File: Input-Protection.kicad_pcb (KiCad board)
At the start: 2 copper layers, 39 parts, among them IC501 AZV3002S-13, J101 EBWA-02-B, J102 KLDX-0202-B, J103 EBWA-02-B, J104 KLDX-0202-B, Q101 MCU18P10Y-TP, Q401 BC846, Q402 MCU18P10Y-TP, U301 LM4040DBZ-5

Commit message: fix: reset pcb layout
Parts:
- removed D101, D401: D3Z10BF-7, Diode_SMD:D_SOD-323_HandSoldering
- removed D501, D502: 1N4148WS, Diode_SMD:D_SOD-323
- removed IC501: AZV3002S-13, Package_SO:Diodes_SO-8EP
- removed ID601: BOARD_STACKUP_MARKER, RD-Symbols-Silkscreen:STACKUP_ID_2L_SML
- removed J101, J103: EBWA-02-B, TerminalBlock_Phoenix:TerminalBlock_Phoenix_MKDS-1-2-3.81_1x02_P3.81mm_Horizontal
- removed J102, J104: KLDX-0202-B, Connector_BarrelJack:BarrelJack_Kycon_KLDX-0202-xC_Horizontal
- removed Q101, Q402: MCU18P10Y-TP, MCU18P10Y-TP:DPAK_MCC
- removed Q401: BC846, Package_TO_SOT_SMD:SOT-23
- removed R101, R102, R402, R403, R503: 100k, Resistor_SMD:R_1206_3216Metric_Pad1.30x1.75mm_HandSolder
- removed R201: 39k, Resistor_SMD:R_1206_3216Metric_Pad1.30x1.75mm_HandSolder
- removed R202, R204, R301, R302, R303, R401: 10k, Resistor_SMD:R_1206_3216Metric_Pad1.30x1.75mm_HandSolder
- removed R203: 58k, Resistor_SMD:R_1206_3216Metric_Pad1.30x1.75mm_HandSolder
- removed R404, R504, R505: 1M, Resistor_SMD:R_1206_3216Metric_Pad1.30x1.75mm_HandSolder
- removed R501, R502: 1k, Resistor_SMD:R_1206_3216Metric_Pad1.30x1.75mm_HandSolder
- removed TP101: VIN, TestPoint:TestPoint_Pad_D2.5mm
- removed TP102: VPROT, TestPoint:TestPoint_Pad_D2.5mm
- removed TP201: V_OV, TestPoint:TestPoint_Pad_D2.5mm
- removed TP202: V_UV, TestPoint:TestPoint_Pad_D2.5mm
- removed TP301: VREF_2V5, TestPoint:TestPoint_Pad_D2.5mm
- removed TP302: VCC_5V, TestPoint:TestPoint_Pad_D2.5mm
- removed TP401: VOUT, TestPoint:TestPoint_Pad_D2.5mm
- removed U301: LM4040DBZ-5, Package_TO_SOT_SMD:SOT-23

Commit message: feat: Added some design notes, fixed some values in line with sim
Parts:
- added C401: 10n, Capacitor_SMD:C_0603_1608Metric_Pad1.08x0.95mm_HandSolder, F.Cu at (170.5, 61.3)
- added C402: 100n, Capacitor_SMD:C_0603_1608Metric_Pad1.08x0.95mm_HandSolder, F.Cu at (170.5, 63.8)
- added C601: 10n, Capacitor_SMD:C_0603_1608Metric_Pad1.08x0.95mm_HandSolder, F.Cu at (170.5, 66.3)
- added C602: 10n, Capacitor_SMD:C_0603_1608Metric_Pad1.08x0.95mm_HandSolder, F.Cu at (170.5, 68.8)
- added D201: D3Z10BF-7, Diode_SMD:D_SOD-323_HandSoldering, F.Cu at (135.0, 98.9)
- added D501: D3Z10BF-7, Diode_SMD:D_SOD-323_HandSoldering, F.Cu at (135.0, 101.9)
- added D701: 1N4148WS, Diode_SMD:D_SOD-323, F.Cu at (139.7, 98.9)
- added D702: 1N4148WS, Diode_SMD:D_SOD-323, F.Cu at (139.7, 101.9)
- added FID901: FIDUCIAL, Fiducial:Fiducial_Cross_0.5mm_Mask2mm, F.Cu at (153.5, 78.3)
- added FID902: FIDUCIAL, Fiducial:Fiducial_Cross_0.5mm_Mask2mm, F.Cu at (153.5, 81.9)
- added FID903: FIDUCIAL, Fiducial:Fiducial_Cross_0.5mm_Mask2mm, F.Cu at (153.5, 85.4)
- added H901: MOUNT_M3, MountingHole:MountingHole_3.2mm_M3_ISO7380_Pad, F.Cu at (148.1, 80.2)
- added H902: MOUNT_M3, MountingHole:MountingHole_3.2mm_M3_ISO7380_Pad, F.Cu at (148.1, 87.4)
- added H903: MOUNT_M3, MountingHole:MountingHole_3.2mm_M3_ISO7380_Pad, F.Cu at (148.1, 94.7)
- added H904: MOUNT_M3, MountingHole:MountingHole_3.2mm_M3_ISO7380_Pad, F.Cu at (148.1, 101.9)
- added ID901: BOARD_STACKUP_MARKER, RD-Symbols-Silkscreen:STACKUP_ID_2L_SML, F.Cu at (165.0, 104.0)
- added J101: KLDX-0202-B, Connector_BarrelJack:BarrelJack_Kycon_KLDX-0202-xC_Horizontal, F.Cu at (142.5, 65.5)
- added J102: EBWA-02-B, TerminalBlock_Phoenix:TerminalBlock_Phoenix_MKDS-1-2-3.81_1x02_P3.81mm_Horizontal, F.Cu at (165.3, 81.3)
- added J103: EBWA-02-B, TerminalBlock_Phoenix:TerminalBlock_Phoenix_MKDS-1-2-3.81_1x02_P3.81mm_Horizontal, F.Cu at (165.3, 90.9)
- added J104: KLDX-0202-B, Connector_BarrelJack:BarrelJack_Kycon_KLDX-0202-xC_Horizontal, F.Cu at (142.5, 77.8)
- added Q201: MCU18P10Y-TP, MCU18P10Y-TP:DPAK_MCC, F.Cu at (131.7, 90.3)
- added Q501: BC846, Package_TO_SOT_SMD:SOT-23, F.Cu at (130.0, 99.7)
- added Q502: MCU18P10Y-TP, MCU18P10Y-TP:DPAK_MCC, F.Cu at (140.1, 90.3)
- added R201: 100k, Resistor_SMD:R_1206_3216Metric_Pad1.30x1.75mm_HandSolder, F.Cu at (147.5, 61.7)
- added R202: 100k, Resistor_SMD:R_1206_3216Metric_Pad1.30x1.75mm_HandSolder, F.Cu at (147.5, 65.0)
- added R301: 39.2k, Resistor_SMD:R_1206_3216Metric_Pad1.30x1.75mm_HandSolder, F.Cu at (147.5, 68.3)
- added R302: 10k, Resistor_SMD:R_1206_3216Metric_Pad1.30x1.75mm_HandSolder, F.Cu at (147.5, 71.6)
- added R303: 56.2k, Resistor_SMD:R_1206_3216Metric_Pad1.30x1.75mm_HandSolder, F.Cu at (147.5, 74.9)
- added R304: 10k, Resistor_SMD:R_1206_3216Metric_Pad1.30x1.75mm_HandSolder, F.Cu at (153.4, 61.7)
- added R401: 100k, Resistor_SMD:R_1206_3216Metric_Pad1.30x1.75mm_HandSolder, F.Cu at (153.4, 65.0)
- added R402: 100k, Resistor_SMD:R_1206_3216Metric_Pad1.30x1.75mm_HandSolder, F.Cu at (153.4, 68.3)
- added R403: 10k, Resistor_SMD:R_1206_3216Metric_Pad1.30x1.75mm_HandSolder, F.Cu at (153.4, 71.6)
- added R501: 10k, Resistor_SMD:R_1206_3216Metric_Pad1.30x1.75mm_HandSolder, F.Cu at (153.4, 74.9)
- added R502: 100k, Resistor_SMD:R_1206_3216Metric_Pad1.30x1.75mm_HandSolder, F.Cu at (159.4, 61.7)
- added R503: 100k, Resistor_SMD:R_1206_3216Metric_Pad1.30x1.75mm_HandSolder, F.Cu at (159.4, 65.0)
- added R504: 1M, Resistor_SMD:R_1206_3216Metric_Pad1.30x1.75mm_HandSolder, F.Cu at (159.4, 68.3)
- added R601: 1k, Resistor_SMD:R_1206_3216Metric_Pad1.30x1.75mm_HandSolder, F.Cu at (159.4, 71.6)
- added R602: 1k, Resistor_SMD:R_1206_3216Metric_Pad1.30x1.75mm_HandSolder, F.Cu at (159.4, 74.9)
- added R701: 470, Resistor_SMD:R_1206_3216Metric_Pad1.30x1.75mm_HandSolder, F.Cu at (165.3, 61.7)
- added R702: 470, Resistor_SMD:R_1206_3216Metric_Pad1.30x1.75mm_HandSolder, F.Cu at (165.3, 65.0)
- added R703: 47k, Resistor_SMD:R_1206_3216Metric_Pad1.30x1.75mm_HandSolder, F.Cu at (165.3, 68.3)
- added R801: 1M, Resistor_SMD:R_1206_3216Metric_Pad1.30x1.75mm_HandSolder, F.Cu at (165.3, 71.6)
- added R802: 1M, Resistor_SMD:R_1206_3216Metric_Pad1.30x1.75mm_HandSolder, F.Cu at (165.3, 74.9)
- added TP101: GND, TestPoint:TestPoint_Pad_D1.5mm, F.Cu at (153.5, 89.0)
- added TP102: VIN, TestPoint:TestPoint_Pad_D1.5mm, F.Cu at (153.5, 92.5)
- added TP103: VOUT, TestPoint:TestPoint_Pad_D1.5mm, F.Cu at (153.5, 96.1)
- added TP104: GND, TestPoint:TestPoint_Pad_D1.5mm, F.Cu at (157.1, 78.3)
- added TP202: VPROT, TestPoint:TestPoint_Pad_D1.5mm, F.Cu at (157.1, 81.9)
- added TP301: GND, TestPoint:TestPoint_Pad_D1.5mm, F.Cu at (157.1, 85.4)
- added TP302: VSENSE_12V, TestPoint:TestPoint_Pad_D1.5mm, F.Cu at (157.1, 89.0)
- added TP303: VSENSE_17V, TestPoint:TestPoint_Pad_D1.5mm, F.Cu at (157.1, 92.5)
- added TP401: VREF_2V5, TestPoint:TestPoint_Pad_D1.5mm, F.Cu at (157.1, 96.1)
- added TP402: VCC_5V, TestPoint:TestPoint_Pad_D1.5mm, F.Cu at (160.6, 78.3)
- added TP403: GND, TestPoint:TestPoint_Pad_D1.5mm, F.Cu at (160.6, 81.9)
- added TP601: 12V_OK, TestPoint:TestPoint_Pad_D1.5mm, F.Cu at (160.6, 85.4)
- added TP602: 17V_OK, TestPoint:TestPoint_Pad_D1.5mm, F.Cu at (160.6, 89.0)
- added TP701: EN_OK, TestPoint:TestPoint_Pad_D1.5mm, F.Cu at (160.6, 92.5)
- added U401: LM4040DBZ-5, Package_TO_SOT_SMD:SOT-23, F.Cu at (130.0, 104.1)
- added U601: AZV3002S-13, Package_SO:Diodes_SO-8EP, F.Cu at (166.4, 99.3)

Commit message: feat: preliminary pcb layout
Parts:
- removed C601, C602: 10n, Capacitor_SMD:C_0603_1608Metric_Pad1.08x0.95mm_HandSolder
- removed D701, D702: 1N4148WS, Diode_SMD:D_SOD-323
- removed Q501: BC846, Package_TO_SOT_SMD:SOT-23
- removed Q502: MCU18P10Y-TP, MCU18P10Y-TP:DPAK_MCC
- removed R701, R702: 470, Resistor_SMD:R_1206_3216Metric_Pad1.30x1.75mm_HandSolder
- removed R703: 47k, Resistor_SMD:R_1206_3216Metric_Pad1.30x1.75mm_HandSolder
- removed R801, R802: 1M, Resistor_SMD:R_1206_3216Metric_Pad1.30x1.75mm_HandSolder
- removed TP202: VPROT, TestPoint:TestPoint_Pad_D1.5mm
- removed TP402: VCC_5V, TestPoint:TestPoint_Pad_D1.5mm
- removed TP601: 12V_OK, TestPoint:TestPoint_Pad_D1.5mm
- removed TP602: 17V_OK, TestPoint:TestPoint_Pad_D1.5mm
- removed TP701: EN_OK, TestPoint:TestPoint_Pad_D1.5mm
- removed U601: AZV3002S-13, Package_SO:Diodes_SO-8EP
- added C501: 10n, Capacitor_SMD:C_0603_1608Metric_Pad1.08x0.95mm_HandSolder, F.Cu at (161.0, 87.7)
- added C502: 10n, Capacitor_SMD:C_0603_1608Metric_Pad1.08x0.95mm_HandSolder, F.Cu at (161.0, 77.5)
- added D502: 1N4148WS, Diode_SMD:D_SOD-323, F.Cu at (155.6, 93.3)
- added D601: D3Z10BF-7, Diode_SMD:D_SOD-323_HandSoldering, F.Cu at (171.6, 85.7)
- added Q601: BC846, Package_TO_SOT_SMD:SOT-23, F.Cu at (169.1, 94.8)
- added Q602: MCU18P10Y-TP, MCU18P10Y-TP:DPAK_MCC, F.Cu at (171.6, 77.4)
- added R505: 47k, Resistor_SMD:R_1206_3216Metric_Pad1.30x1.75mm_HandSolder, F.Cu at (148.6, 89.2)
- added R506: 1M, Resistor_SMD:R_1206_3216Metric_Pad1.30x1.75mm_HandSolder, F.Cu at (152.6, 89.2)
- added R507: 1M, Resistor_SMD:R_1206_3216Metric_Pad1.30x1.75mm_HandSolder, F.Cu at (152.6, 75.9)
- added R603: 100k, Resistor_SMD:R_1206_3216Metric_Pad1.30x1.75mm_HandSolder, F.Cu at (171.6, 90.7)
- added R604: 1M, Resistor_SMD:R_1206_3216Metric_Pad1.30x1.75mm_HandSolder, F.Cu at (171.6, 68.2)
- added TP201: VPROT, TestPoint:TestPoint_Pad_D1.5mm, F.Cu at (133.1, 94.7)
- added TP501: 12V_OK, TestPoint:TestPoint_Pad_D1.0mm, F.Cu at (152.1, 85.4)
- added TP502: 17V_OK, TestPoint:TestPoint_Pad_D1.0mm, F.Cu at (153.2, 72.4)
- added TP503: EN_OK, TestPoint:TestPoint_Pad_D1.5mm, F.Cu at (169.1, 98.9)
- added U501: AZV3002S-13, Package_SO:Diodes_SO-8EP, F.Cu at (157.3, 82.5)
- D501: value D3Z10BF-7 -> 1N4148WS; footprint Diode_SMD:D_SOD-323_HandSoldering -> Diode_SMD:D_SOD-323
- R501: value 10k -> 1k
- R502: value 100k -> 1k
- R503: value 100k -> 470
- R504: value 1M -> 470
- R601: value 1k -> 10k
- R602: value 1k -> 100k
- TP101, TP104, TP301: footprint TestPoint:TestPoint_Pad_D1.5mm -> TestPoint:TestPoint_THTPad_2.0x2.0mm_Drill1.0mm
- TP401: footprint TestPoint:TestPoint_Pad_D1.5mm -> TestPoint:TestPoint_Pad_D1.0mm
- TP403: value GND -> VCC_5V; footprint TestPoint:TestPoint_Pad_D1.5mm -> TestPoint:TestPoint_Pad_D1.0mm
- U401: value LM4040DBZ-5 -> LM4040N-5.0
- moved ID901 55.9 mm to (124.3, 65.7)
- moved H903 49.0 mm to (187.6, 65.7)
- moved J102 48.9 mm to (116.6, 85.7), turned to -90 degrees
- moved H904 39.7 mm to (187.6, 97.7)
- moved R201 38.1 mm to (128.5, 94.7)
- moved FID902 36.5 mm to (120.6, 97.7)
- moved D501 36.5 mm to (155.6, 71.7), turned to 90 degrees
- moved H901 35.7 mm to (115.6, 65.7)
- moved FID901 35.3 mm to (120.6, 65.7)
- moved FID903 35.1 mm to (182.6, 65.7)
- moved J104 34.5 mm to (176.9, 75.2), turned to 180 degrees
- moved H902 34.1 mm to (115.6, 97.7)
- moved C402 31.1 mm to (146.4, 83.4), turned to -90 degrees
- moved R202 30.2 mm to (131.6, 90.7)
- moved TP102 29.2 mm to (125.3, 84.8), turned to 180 degrees
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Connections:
- net VIN renamed /ARCHITECTURE/1. INTERCONNECTS/VIN
- D201 pad 1: VPROT -> /ARCHITECTURE/2. POLARITY PROTECTION/VPROT
- D501 pad 1: VPROT -> Net-(D501-K)
- D501 pad 2: Net-(D501-A) -> /ARCHITECTURE/5. COMPARATOR/EN_OK
- J103 pad 1: VOUT -> GND
- J103 pad 2: GND -> /ARCHITECTURE/1. INTERCONNECTS/VOUT
- J104 pad 1: VOUT -> /ARCHITECTURE/1. INTERCONNECTS/VOUT
- Q201 pad 3: VPROT -> /ARCHITECTURE/2. POLARITY PROTECTION/VPROT
- R202 pad 2: VPROT -> /ARCHITECTURE/2. POLARITY PROTECTION/VPROT
- R301 pad 1: VSENSE_12V -> /ARCHITECTURE/3. SENSING/VSENSE_12V
- R301 pad 2: VPROT -> /ARCHITECTURE/2. POLARITY PROTECTION/VPROT
- R302 pad 2: VSENSE_12V -> /ARCHITECTURE/3. SENSING/VSENSE_12V
- R303 pad 1: VSENSE_17V -> /ARCHITECTURE/3. SENSING/VSENSE_17V
- R303 pad 2: VPROT -> /ARCHITECTURE/2. POLARITY PROTECTION/VPROT
- R304 pad 2: VSENSE_17V -> /ARCHITECTURE/3. SENSING/VSENSE_17V
- R403 pad 2: VPROT -> /ARCHITECTURE/2. POLARITY PROTECTION/VPROT
- R501 pad 1: Net-(Q501-B) -> Net-(U501A-+)
- R501 pad 2: EN_OK -> /ARCHITECTURE/3. SENSING/VSENSE_12V
- R502 pad 1: Net-(Q501-B) -> Net-(U501B--)
- R502 pad 2: GND -> /ARCHITECTURE/3. SENSING/VSENSE_17V
- R503 pad 1: Net-(D501-A) -> Net-(D501-K)
- R503 pad 2: VPROT -> /ARCHITECTURE/5. COMPARATOR/17V_OK
- R504 pad 1: VOUT -> Net-(D502-K)
- R504 pad 2: GND -> /ARCHITECTURE/5. COMPARATOR/12V_OK
- R601 pad 1: Net-(U601A-+) -> Net-(Q601-B)
- R601 pad 2: VSENSE_12V -> /ARCHITECTURE/5. COMPARATOR/EN_OK
- R602 pad 1: Net-(U601B--) -> Net-(Q601-B)
- R602 pad 2: VSENSE_17V -> GND
- TP103 pad 1: VOUT -> /ARCHITECTURE/1. INTERCONNECTS/VOUT
- TP302 pad 1: VSENSE_12V -> /ARCHITECTURE/3. SENSING/VSENSE_12V
- TP303 pad 1: VSENSE_17V -> /ARCHITECTURE/3. SENSING/VSENSE_17V
- TP403 pad 1: GND -> VCC_5V
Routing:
- net /ARCHITECTURE/5. COMPARATOR/EN_OK: track 0.00 -> 59.5 mm
- net VREF_2V5: track 0.00 -> 31.8 mm
- net /ARCHITECTURE/3. SENSING/VSENSE_17V: track 0.00 -> 22.6 mm
- net /ARCHITECTURE/3. SENSING/VSENSE_12V: track 0.00 -> 20.3 mm
- net GND: track 0.00 -> 10.2 mm, vias 0 -> 8
- net /ARCHITECTURE/5. COMPARATOR/17V_OK: track 0.00 -> 5.98 mm
- net /ARCHITECTURE/5. COMPARATOR/12V_OK: track 0.00 -> 3.49 mm
- net /ARCHITECTURE/2. POLARITY PROTECTION/VPROT: vias 0 -> 6
- added copper zone on F.Cu, net /ARCHITECTURE/1. INTERCONNECTS/VIN
- added copper zone on F.Cu, net /ARCHITECTURE/1. INTERCONNECTS/VOUT
- added copper zone on B.Cu, net /ARCHITECTURE/2. POLARITY PROTECTION/VPROT
- added copper zone on F.Cu, net /ARCHITECTURE/2. POLARITY PROTECTION/VPROT
- added copper zone on F.Cu, net /ARCHITECTURE/3. SENSING/VSENSE_12V
- added copper zone on F.Cu, net /ARCHITECTURE/3. SENSING/VSENSE_17V
- added copper zone on F.Cu, net /ARCHITECTURE/5. COMPARATOR/12V_OK
- added copper zone on F.Cu, net /ARCHITECTURE/5. COMPARATOR/17V_OK
- added copper zone on B.Cu, net GND
- added copper zone on F.Cu, net GND
- added copper zone on F.Cu, net Net-(D201-A)
- added copper zone on F.Cu, net Net-(D501-K)
- added copper zone on F.Cu, net Net-(D502-K)
- added copper zone on F.Cu, net Net-(D601-A)
- added copper zone on F.Cu, net Net-(Q601-B)
- added copper zone on F.Cu, net Net-(U501A-+)
- added copper zone on F.Cu, net Net-(U501B--)
- added copper zone on F.Cu, net VCC_5V
- added copper zone on F.Cu, net VREF_2V5
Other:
- board outline added: 80 x 40 mm
- board text added: "A"
- board text added: "INPUT PROTECTION"
- board text added: "MAX -50 to +50 V ON INPUT ONLY"
- board text added: "REV"

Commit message: fix: template issue
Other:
- board text removed: "Impedance Table"

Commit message: fix: test point changes
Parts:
- TP101, TP104, TP301: footprint TestPoint:TestPoint_THTPad_2.0x2.0mm_Drill1.0mm -> RD-Testpoints:TestPoint_THTPad_1.5x1.5mm_Drill0.7mm
- TP102, TP103, TP201, TP302, TP303, TP503: footprint TestPoint:TestPoint_Pad_D1.5mm -> RD-Testpoints:TestPoint_Pad_D1.5mm
- TP401, TP403, TP501, TP502: footprint TestPoint:TestPoint_Pad_D1.0mm -> RD-Testpoints:TestPoint_Pad_D1.0mm
- moved TP401 6.00 mm to (156.3, 69.2)
- moved C401 6.00 mm to (152.6, 74.3)
- moved C402 6.00 mm to (152.4, 83.4)
- moved C501 6.00 mm to (167.0, 87.7)
- moved C502 6.00 mm to (167.0, 77.5)
- moved D201 6.00 mm to (137.6, 85.7)
- moved D501 6.00 mm to (161.6, 71.7)
- moved D502 6.00 mm to (161.6, 93.3)
- moved D601 6.00 mm to (177.6, 85.7)
- moved FID901 6.00 mm to (126.6, 65.7)
- moved FID902 6.00 mm to (126.6, 97.7)
- moved FID903 6.00 mm to (188.6, 65.7)
- moved H901 6.00 mm to (121.6, 65.7)
- moved H902 6.00 mm to (121.6, 97.7)
- moved H903 6.00 mm to (193.6, 65.7)
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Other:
- board text added: "INPUT"
- board text added: "OUTPUT"
- board text added: "V+"
- board text added: "V-"
- board text removed: "30°"
- board text removed: "3× 120°"

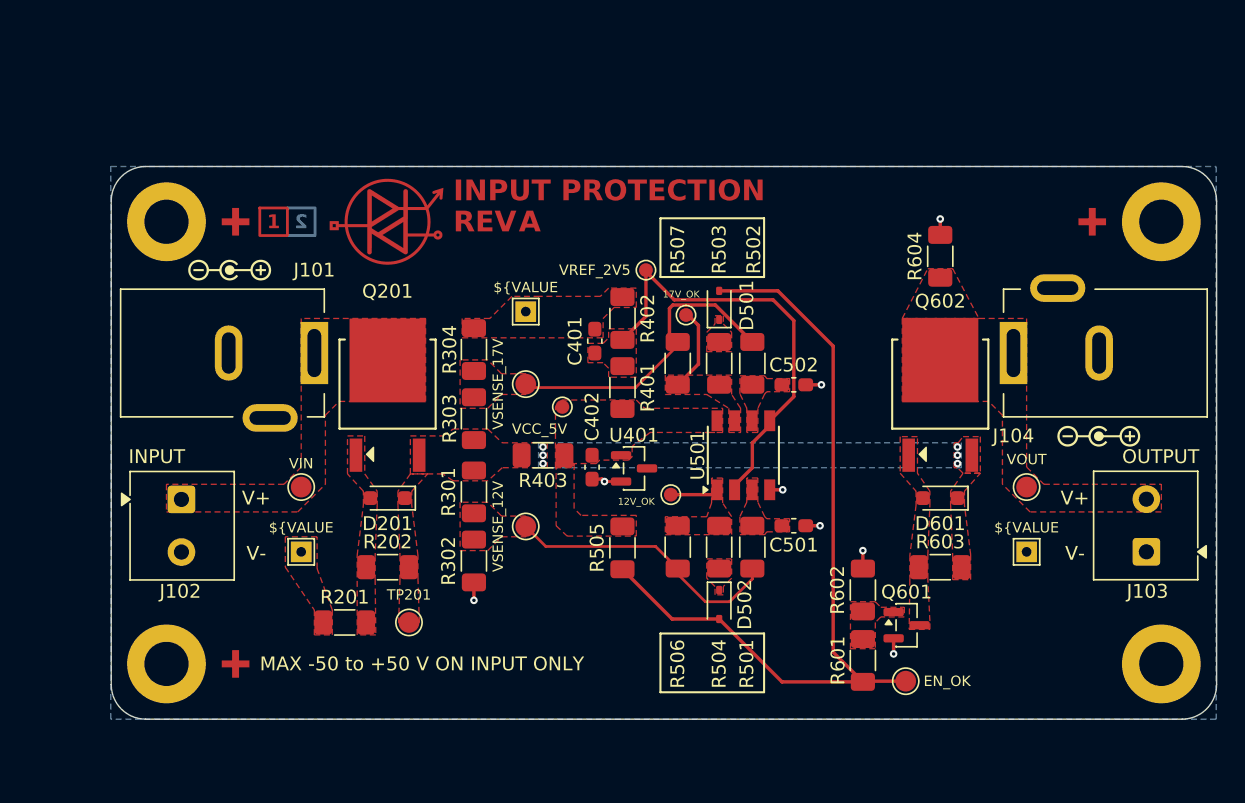
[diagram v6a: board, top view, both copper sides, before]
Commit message: feat: ERC/DRC checks
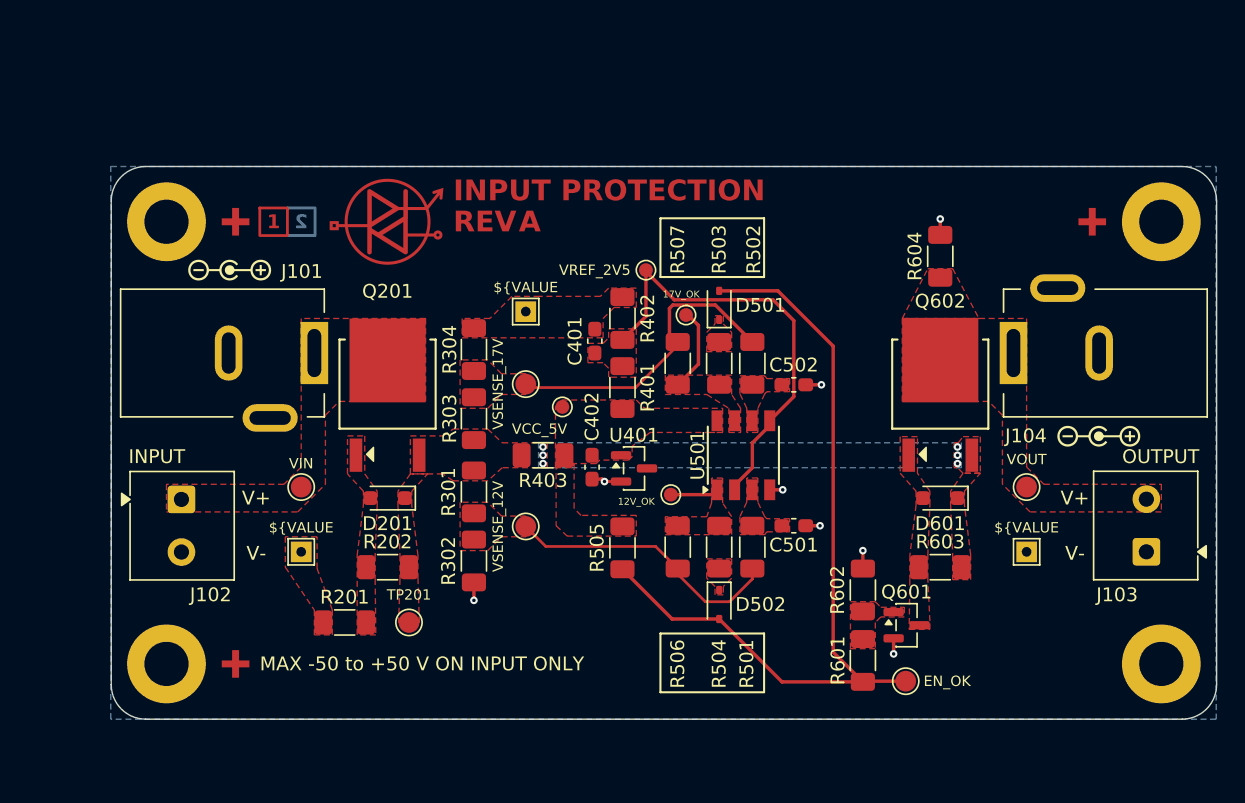
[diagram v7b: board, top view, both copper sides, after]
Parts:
- U501: footprint Package_SO:Diodes_SO-8EP -> AZV3002S-13:Diodes_SO-8EP
